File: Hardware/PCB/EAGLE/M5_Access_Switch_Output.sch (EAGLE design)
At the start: 11 parts, among them K1 G3VM-41AY1, K2 G3VM-41AY1

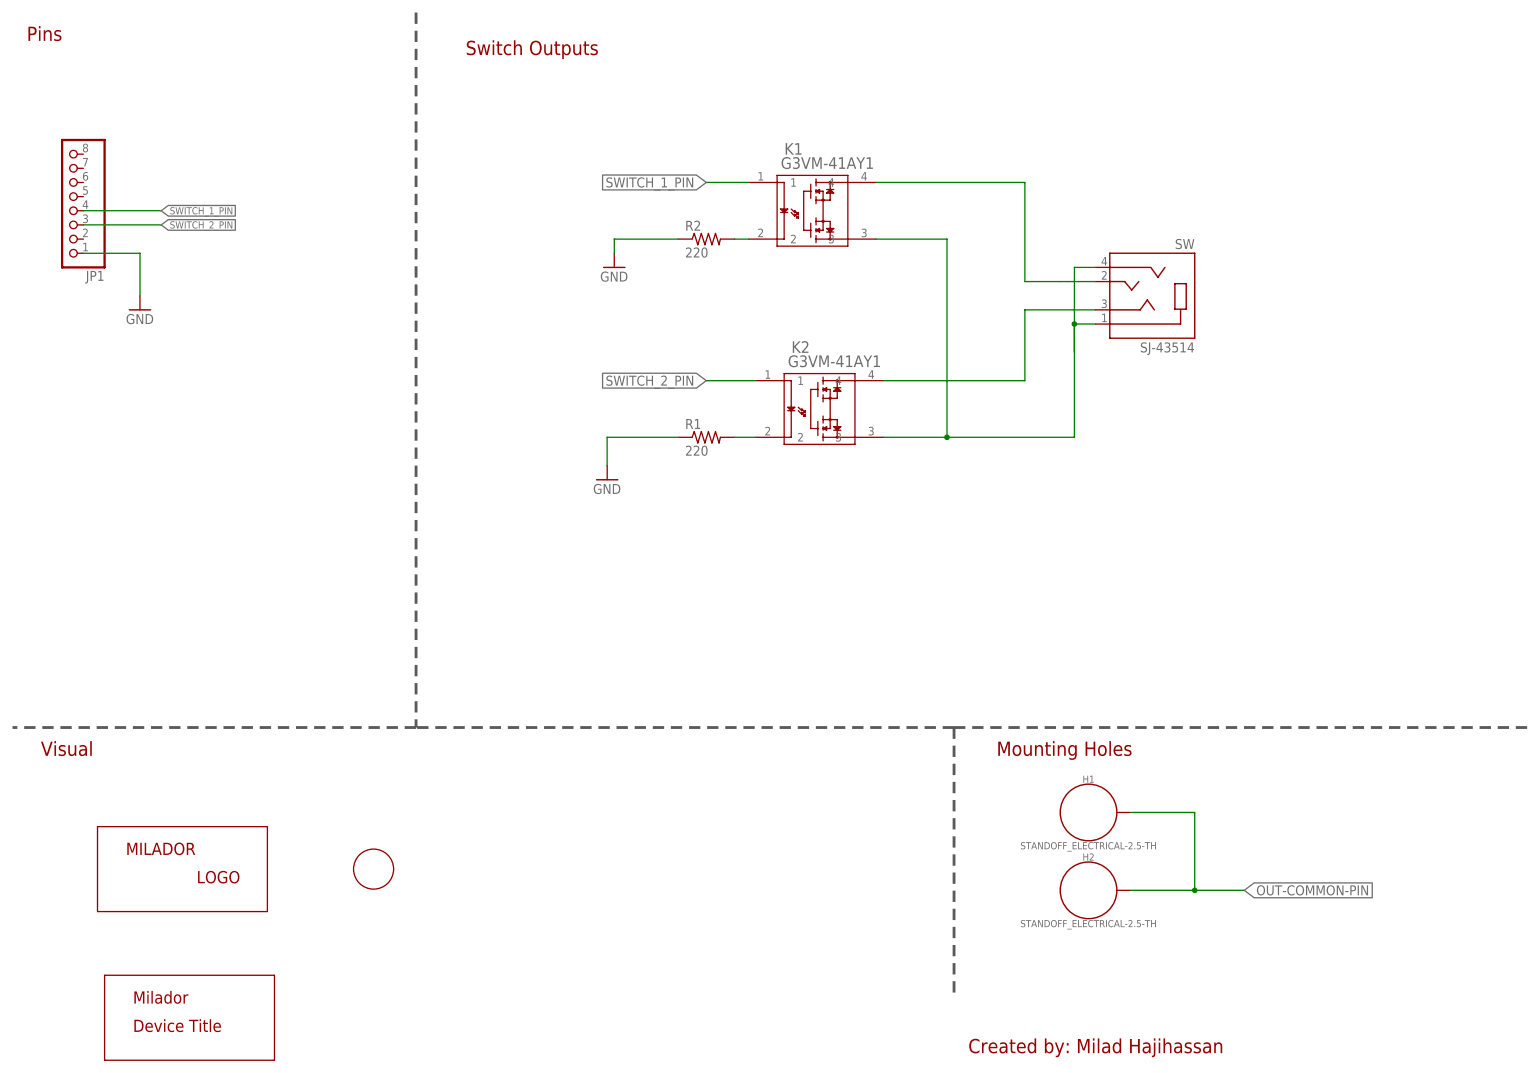
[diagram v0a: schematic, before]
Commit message: Updated design to two mono jack design
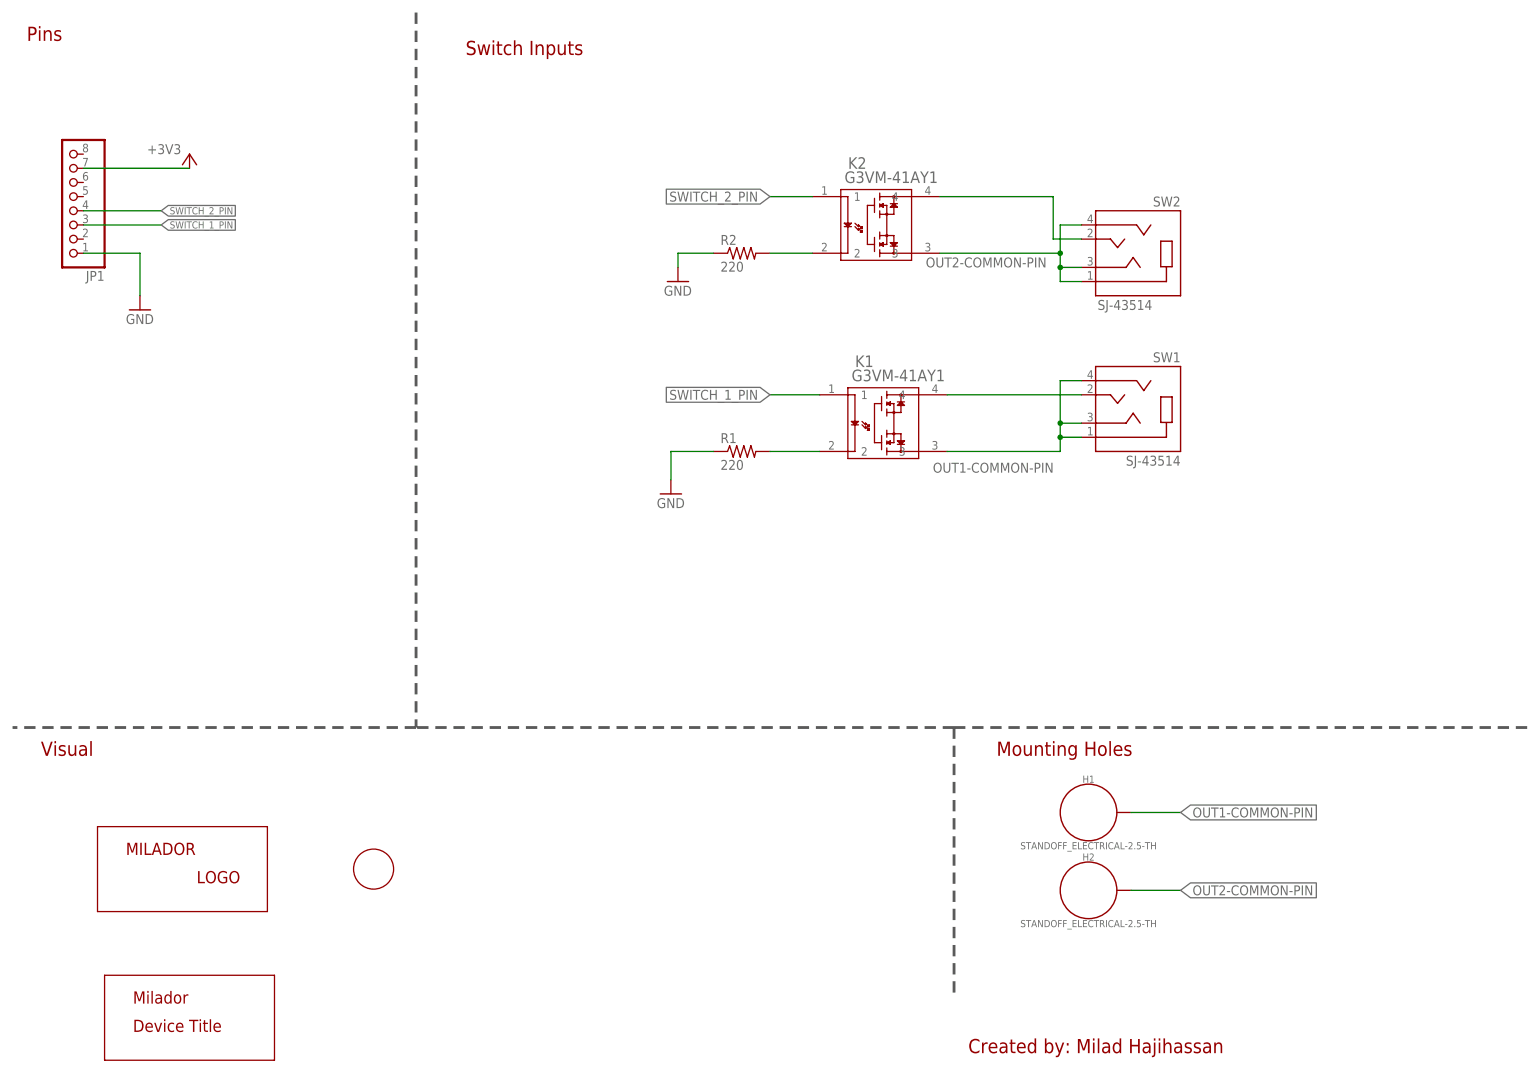
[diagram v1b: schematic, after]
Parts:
- removed SW: SJ-43514, milador:SJ-43514
- added SW1, SW2: SJ-43514, milador:SJ-43514
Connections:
- removed net N$1: K2.2, R1.2
- removed net N$4: K1.2, R2.2
- removed net OUT-COMMON-PIN: H1.P$1, H2.P$1, K1.3, K2.3, SW.RING2, SW.SLEEVE
- new net +3V3: JP1.7
- new net N$2: K2.2, R2.2
- new net N$3: K1.2, R1.2
- new net OUT1-COMMON-PIN: H1.P$1, K1.3, SW1.RING1, SW1.RING2, SW1.SLEEVE
- new net OUT2-COMMON-PIN: H2.P$1, K2.3, SW2.RING1, SW2.RING2, SW2.SLEEVE
- net OUT-1-PIN: now also K2.4, SW2.TIP; no longer K1.4, SW.TIP
- net OUT-2-PIN: now also K1.4, SW1.TIP; no longer K2.4, SW.RING1
- net SWITCH_1_PIN: now also JP1.3; no longer JP1.4
- net SWITCH_2_PIN: now also JP1.4; no longer JP1.3
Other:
- note added: "Switch Inputs"
- note removed: "Switch Outputs"
- moved on the sheet: K1, K2, R1, R2
